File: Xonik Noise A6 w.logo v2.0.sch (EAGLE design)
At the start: 38 parts, among them IC1 TL074D, T1 NOISE-2N3904

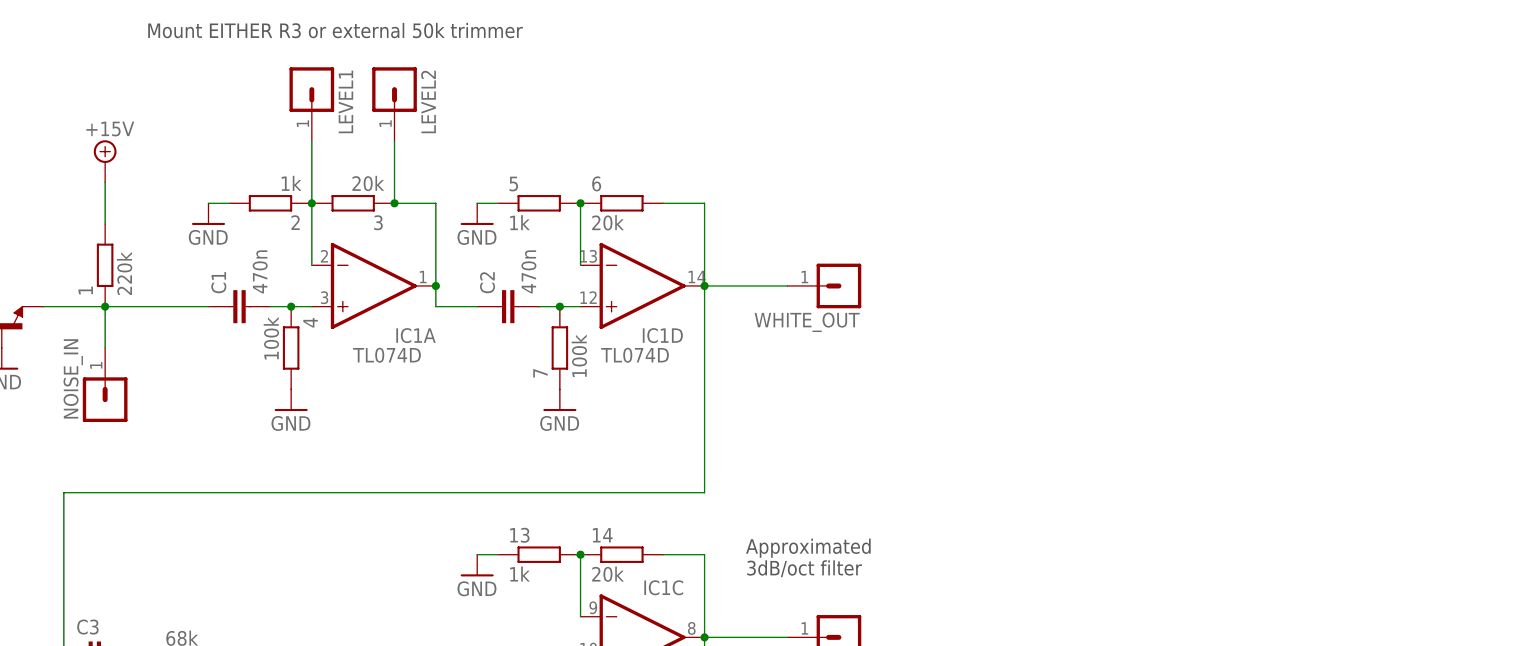
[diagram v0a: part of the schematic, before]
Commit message: Removed default gain resistor and added doc for trimmer
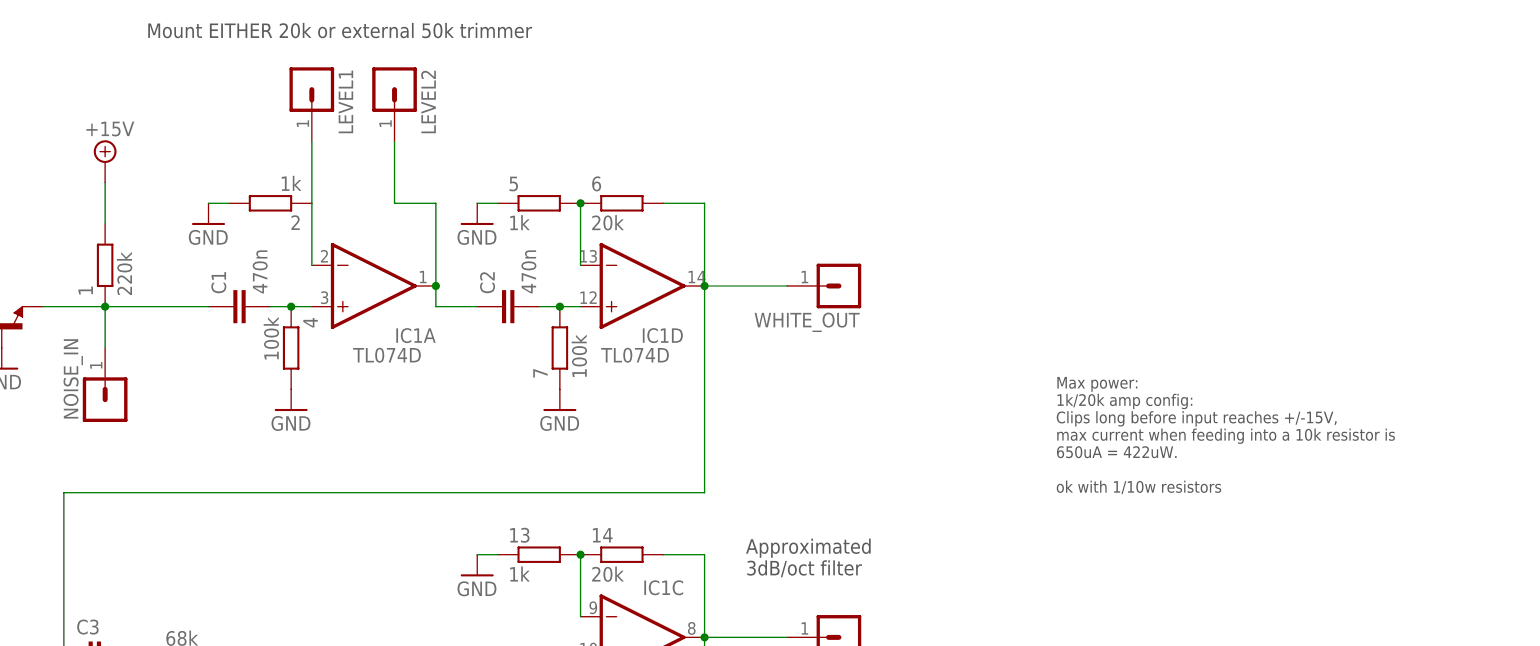
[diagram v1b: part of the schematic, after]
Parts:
- removed 3: 20k, resistor:R-EU_R0805
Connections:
- net N$1: no longer 3.2
- net N$9: no longer 3.1
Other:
- note added: "Max power: 1k/20k amp config: Clips long before input reaches +/-15V, max current when feeding into a 10k resistor is 650uA = 422uW. ok with 1/10w resistors"
- note added: "Mount EITHER 20k or external 50k trimmer"
- note removed: "Mount EITHER R3 or external 50k trimmer"
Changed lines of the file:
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@@
 <part name="1" library="resistor" deviceset="R-EU_" device="R0805" value="220k"/>
 <part name="2" library="resistor" deviceset="R-EU_" device="R0805" value="1k"/>
-<part name="3" library="resistor" deviceset="R-EU_" device="R0805" value="20k"/>
 <part name="4" library="resistor" deviceset="R-EU_" device="R0805" value="100k"/>
 <part name="5" library="resistor" deviceset="R-EU_" device="R0805" value="1k"/>
@@
 <sheet>
 <plain>
-<text x="66.04" y="139.7" size="1.778" layer="97">Mount EITHER R3 or external 50k trimmer</text>
+<text x="66.04" y="139.7" size="1.778" layer="97">Mount EITHER 20k or external 50k trimmer</text>
 <text x="139.7" y="73.66" size="1.778" layer="97">Approximated
 3dB/oct filter</text>
@@
 need to adjust R3.
 </text>
+<text x="177.8" y="83.82" size="1.4224" layer="97">Max power:
+1k/20k amp config:
+Clips long before input reaches +/-15V,
+max current when feeding into a 10k resistor is
+650uA = 422uW.
+ok with 1/10w resistors</text>
 </plain>
 <instances>
@@
 <attribute name="VALUE" x="85.09" y="122.682" size="1.778" layer="96" rot="R180"/>
 </instance>
-<instance part="3" gate="G$1" x="91.44" y="119.38" smashed="yes" rot="R180">
-<attribute name="NAME" x="95.25" y="117.8814" size="1.778" layer="95" rot="R180"/>
-<attribute name="VALUE" x="95.25" y="122.682" size="1.778" layer="96" rot="R180"/>
-</instance>
 <instance part="4" gate="G$1" x="83.82" y="101.6" smashed="yes" rot="R270">
 <attribute name="NAME" x="85.3186" y="105.41" size="1.778" layer="95" rot="R270"/>
@@
 <segment>
 <pinref part="2" gate="G$1" pin="1"/>
-<pinref part="3" gate="G$1" pin="2"/>
 <pinref part="IC1" gate="A" pin="-IN"/>
 <wire x1="86.36" y1="111.76" x2="86.36" y2="119.38" width="0.1524" layer="91"/>
 <pinref part="LEVEL1" gate="G$1" pin="1"/>
 <wire x1="86.36" y1="127" x2="86.36" y2="119.38" width="0.1524" layer="91"/>
-<junction x="86.36" y="119.38"/>
 </segment>
 </net>
@@
 <net name="N$9" class="0">
 <segment>
-<pinref part="3" gate="G$1" pin="1"/>
 <pinref part="IC1" gate="A" pin="OUT"/>
 <wire x1="96.52" y1="119.38" x2="101.6" y2="119.38" width="0.1524" layer="91"/>
@@
 <pinref part="LEVEL2" gate="G$1" pin="1"/>
 <wire x1="96.52" y1="127" x2="96.52" y2="119.38" width="0.1524" layer="91"/>
-<junction x="96.52" y="119.38"/>
 <wire x1="101.6" y1="109.22" x2="101.6" y2="106.68" width="0.1524" layer="91"/>
 <pinref part="C2" gate="G$1" pin="1"/>

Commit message: Added working bom and gerber
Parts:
- 17: value 301k -> 300k
- 9: value 33.2k -> 33k
- C10: value (none) -> 100nF
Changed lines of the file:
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@@
 <part name="7" library="resistor" deviceset="R-EU_" device="R0805" value="100k"/>
 <part name="8" library="resistor" deviceset="R-EU_" device="R0805" value="68k"/>
-<part name="9" library="resistor" deviceset="R-EU_" device="R0805" value="33.2k"/>
+<part name="9" library="resistor" deviceset="R-EU_" device="R0805" value="33k"/>
 <part name="10" library="resistor" deviceset="R-EU_" device="R0805" value="10k"/>
 <part name="11" library="resistor" deviceset="R-EU_" device="R0805" value="3k"/>
@@
 <part name="15" library="resistor" deviceset="R-EU_" device="R0805" value="4k7"/>
 <part name="16" library="resistor" deviceset="R-EU_" device="R0805" value="15k"/>
-<part name="17" library="resistor" deviceset="R-EU_" device="R0805" value="301k"/>
+<part name="17" library="resistor" deviceset="R-EU_" device="R0805" value="300k"/>
 <part name="C1" library="resistor" deviceset="C-EU" device="C0805" value="470n"/>
 <part name="C2" library="resistor" deviceset="C-EU" device="C0805" value="470n"/>
@@
 <part name="C9" library="resistor" deviceset="C-EU" device="C0805" value="2n2"/>
 <part name="IC1" library="linear" deviceset="TL074" device="D"/>
-<part name="C10" library="resistor" deviceset="C-EU" device="C0603"/>
+<part name="C10" library="resistor" deviceset="C-EU" device="C0603" value="100nF"/>
 <part name="NOISE_IN" library="joakim" deviceset="MA01-1J" device="P"/>
 <part name="LEVEL1" library="joakim" deviceset="MA01-1J" device="P"/>

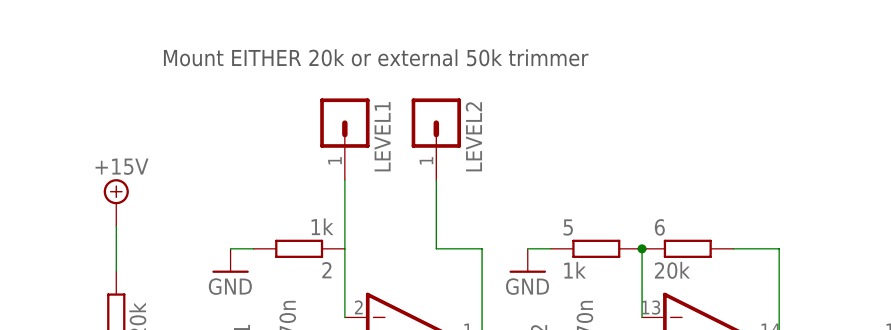
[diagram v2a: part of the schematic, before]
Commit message: Added comment about trimmer
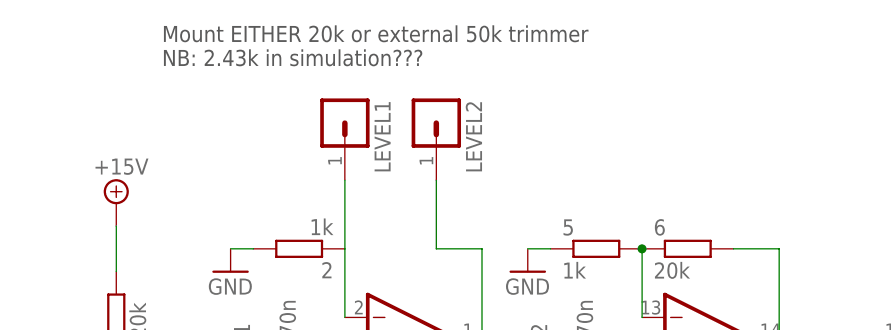
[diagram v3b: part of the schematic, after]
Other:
- note added: "Mount EITHER 20k or external 50k trimmer NB: 2.43k in simulation???"
- note removed: "Mount EITHER 20k or external 50k trimmer"
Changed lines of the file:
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@@
 <sheet>
 <plain>
-<text x="66.04" y="139.7" size="1.778" layer="97">Mount EITHER 20k or external 50k trimmer</text>
+<text x="66.04" y="139.7" size="1.778" layer="97">Mount EITHER 20k or external 50k trimmer
+NB: 2.43k in simulation???</text>
 <text x="139.7" y="73.66" size="1.778" layer="97">Approximated
 3dB/oct filter</text>
